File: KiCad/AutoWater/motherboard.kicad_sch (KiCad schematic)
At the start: 23 parts

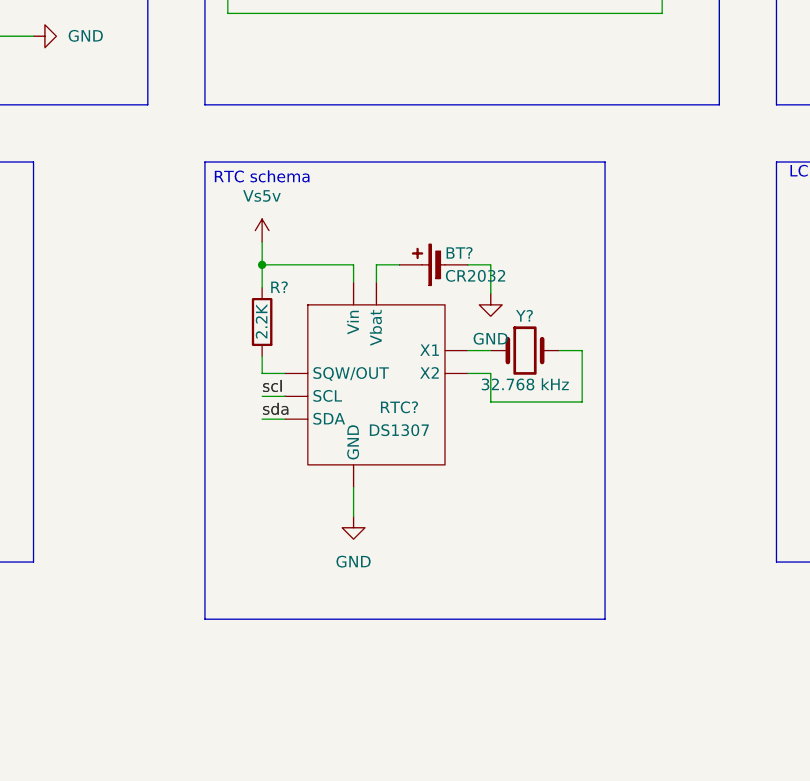
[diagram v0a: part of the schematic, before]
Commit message: Refactor RTC  to module
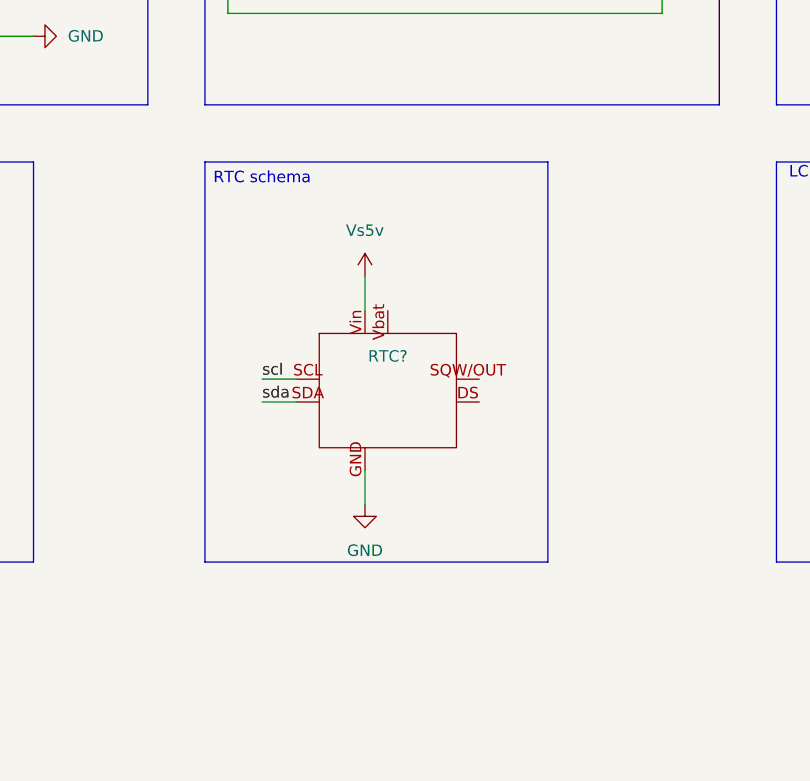
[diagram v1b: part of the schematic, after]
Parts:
- removed BT?: CR2032, symbol AutoWater:Power
- removed R?: 2.2K, symbol AutoWater:Resistor
- removed RTC?: DS1307, symbol AutoWater:RTC DS1307
- removed Y?: 32.768 kHz, symbol AutoWater:Crystal
- added RTC?: ~, symbol AutoWater:RTC DS1307 module
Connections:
- net GND: now also RTC?.GND
- net Vs5v: now also RTC?.Vin
- net scl: now also RTC?.SCL
- net sda: now also RTC?.SDA

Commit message: Create layouts
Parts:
- BT1: renamed from BT?; footprint (none) -> AutoWater:Connector 5.5x2.1 DS-201
- C1, C2: renamed from C?; footprint (none) -> AutoWater:Capacitor Murata SMD 0603
- LCD1: renamed from LCD?; footprint (none) -> AutoWater:PLS-4
- MCU1: renamed from MCU?; footprint (none) -> AutoWater:Arduino Nano V3 Type C PBS
- R1, R2: renamed from R?; footprint (none) -> AutoWater:Resistor Yageo SMD 1206
- RTC1: renamed from RTC?; footprint (none) -> AutoWater:RTC DS1307 module
- SD1: renamed from SD?; footprint (none) -> AutoWater:MicroSD module
- SM1: renamed from SM?; footprint (none) -> AutoWater:PLS-4
- STB1: renamed from STB?; footprint (none) -> AutoWater:Stabilizer 5V AMS1117-5.0S SMD
- SW1, SW2: renamed from SW?; footprint (none) -> AutoWater:Connector B2B-XH-A
- WM1: renamed from WM?; footprint (none) -> AutoWater:PLS-2x3
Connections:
- net GND: now also LCD1.4 (GND), SM1.4 (GND), SW1.GND (1), SW2.GND (1); no longer LCD1.GND, SM1.GND, SW1.1, SW2.1
- net Vs5v: now also LCD1.3 (Vin), SM1.1 (Vin); no longer LCD1.Vin, SM1.Vin
- net scl: now also LCD1.1 (SCL); no longer LCD1.SCL
- net sda: now also LCD1.2 (SDA); no longer LCD1.SDA
- net at MCU1.D3 (PWD): now also SM1.2 (SER); no longer SM1.SER
- net at MCU1.D4: now also SM1.3 (CLK); no longer SM1.CLK
- net at MCU1.D7: now also SW2.Vin (2); no longer SW2.2
- net at MCU1.RST: now also SW1.Vin (2); no longer SW1.2
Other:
- moved on the sheet: MCU1G, SM1
